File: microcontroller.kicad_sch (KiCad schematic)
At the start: 34 parts, among them U1 STM32H745XIH6

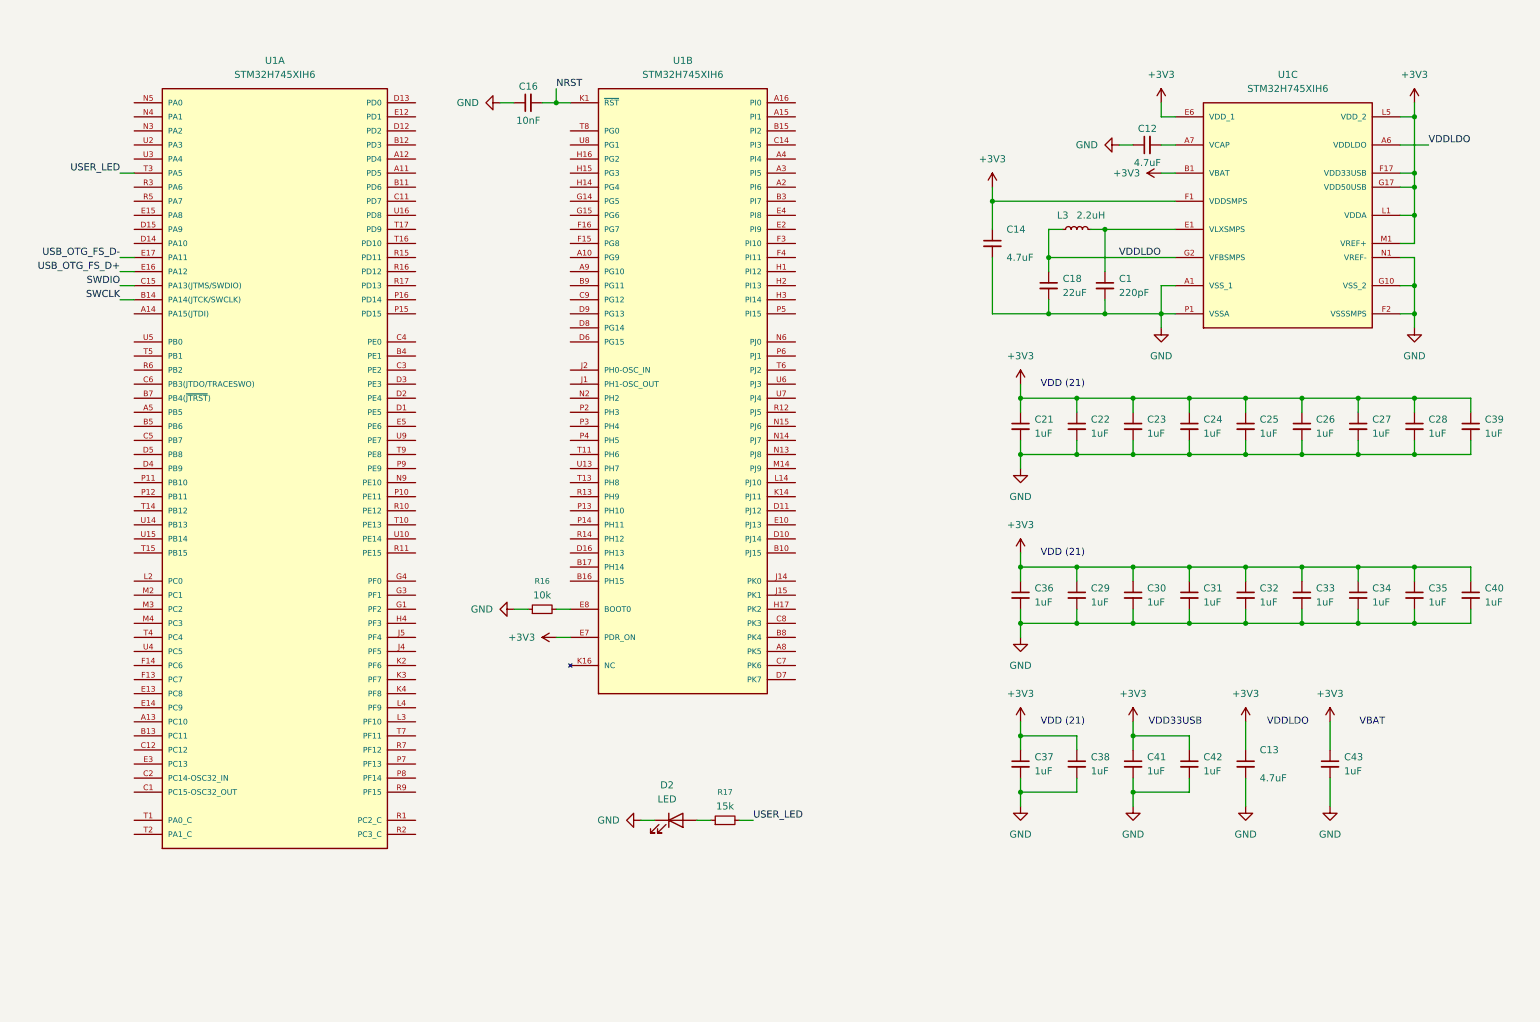
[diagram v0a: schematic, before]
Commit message: add fmc pins, stomp uart, fuel gauge i2c
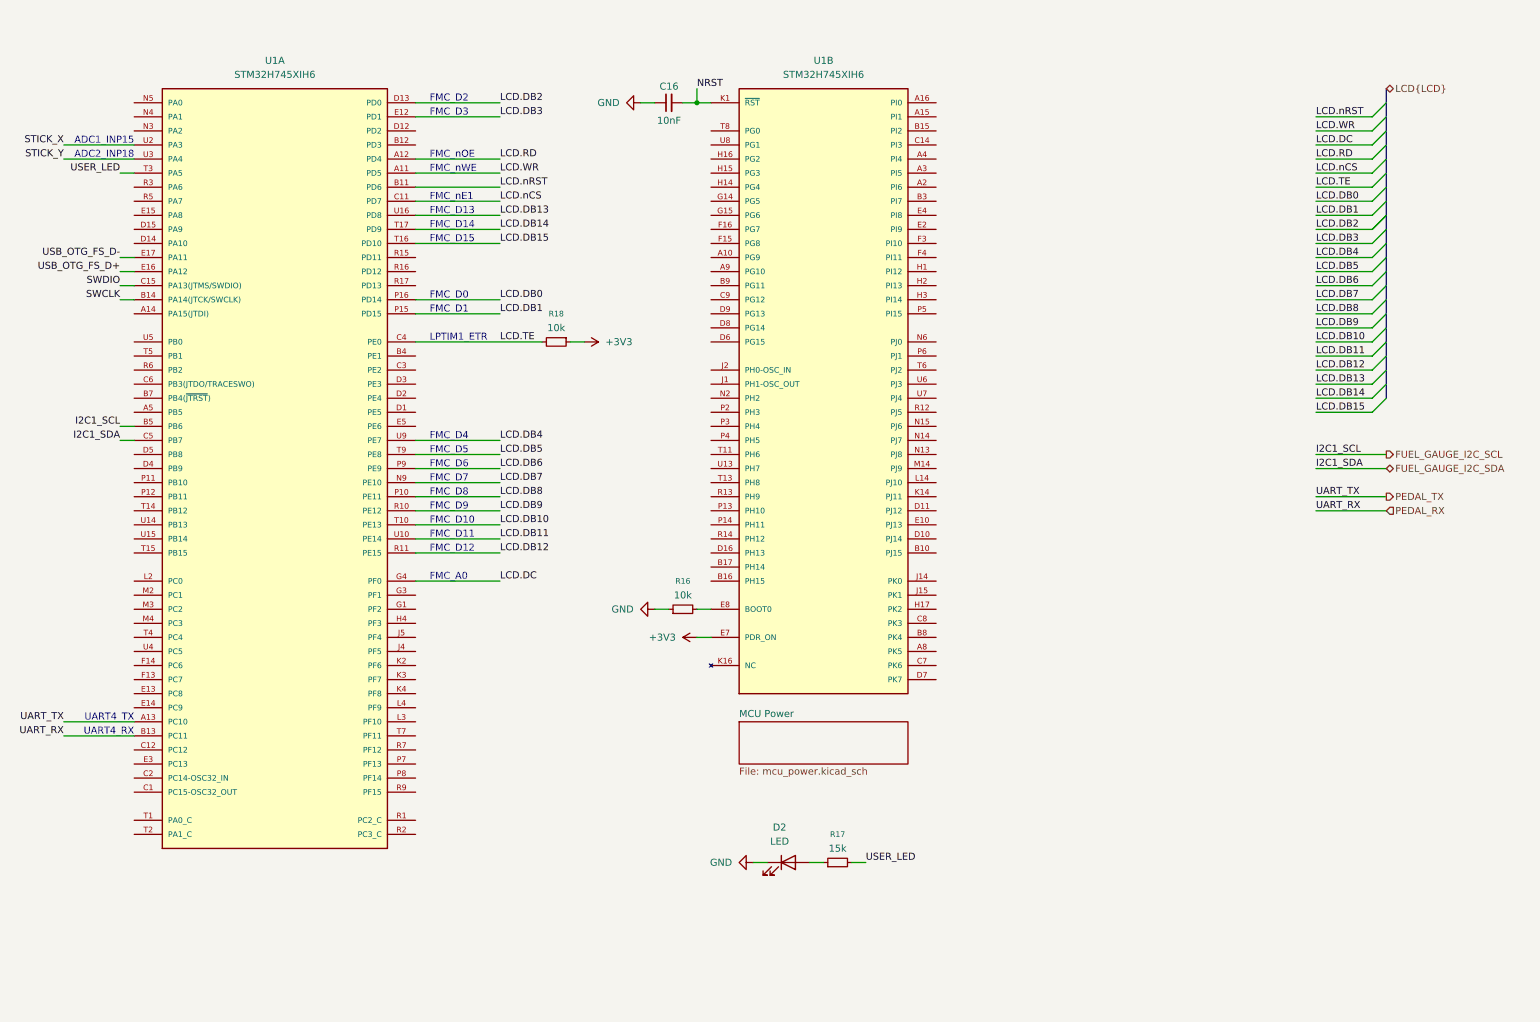
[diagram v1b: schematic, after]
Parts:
- removed C1: 220pF, Capacitor_SMD:C_0402_1005Metric, symbol Device:C_Small
- removed C12, C13, C14: 4.7uF, Capacitor_SMD:C_0402_1005Metric, symbol Device:C_Small
- removed C18: 22uF, Capacitor_SMD:C_0805_2012Metric, symbol Device:C_Small
- removed C21, C22, C23, C24, C25, C26, C27, C28, C29, C30, C31, C32, C33, C34, C35, C36, C37, C38, C39, C40, C41, C42, C43: 1uF, Capacitor_SMD:C_0402_1005Metric, symbol Device:C_Small
- removed L3: 2.2uH, Inductor_SMD:L_0805_2012Metric, symbol Device:L_Small
- removed unit 3 of U1
- added R18: 10k, Resistor_SMD:R_0402_1005Metric, symbol Device:R_Small
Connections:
- net +3V3: now also R18.1
- net LCD.WR: now reaches U1.A11 (PD5)
- net LCD.RD: now reaches U1.A12 (PD4)
- net PEDAL_TX: now reaches U1.A13 (PC10)
- net LCD.nRST: now reaches U1.B11 (PD6)
- net PEDAL_RX: now reaches U1.B13 (PC11)
- net FUEL_GAUGE_I2C_SCL: now reaches U1.B5 (PB6)
- net LCD.nCS: now reaches U1.C11 (PD7)
- net LCD.TE: now reaches U1.C4 (PE0)
- net LCD.TE: now also R18.2
- net FUEL_GAUGE_I2C_SDA: now reaches U1.C5 (PB7)
- net LCD.DB2: now reaches U1.D13 (PD0)
- net LCD.DB3: now reaches U1.E12 (PD1)
- net LCD.DC: now reaches U1.G4 (PF0)
- net LCD.DB7: now reaches U1.N9 (PE10)
- net LCD.DB8: now reaches U1.P10 (PE11)
- net LCD.DB1: now reaches U1.P15 (PD15)
- net LCD.DB0: now reaches U1.P16 (PD14)
- net LCD.DB6: now reaches U1.P9 (PE9)
- net LCD.DB9: now reaches U1.R10 (PE12)
- net LCD.DB12: now reaches U1.R11 (PE15)
- net LCD.DB10: now reaches U1.T10 (PE13)
- net LCD.DB15: now reaches U1.T16 (PD10)
- net LCD.DB14: now reaches U1.T17 (PD9)
- net LCD.DB5: now reaches U1.T9 (PE8)
- net LCD.DB11: now reaches U1.U10 (PE14)
- net LCD.DB13: now reaches U1.U16 (PD8)
- net STICK_X: now reaches U1.U2 (PA3)
- net STICK_Y: now reaches U1.U3 (PA4)
- net LCD.DB4: now reaches U1.U9 (PE7)
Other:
- added sheet MCU Power (mcu_power.kicad_sch)
- note added: "ADC1_INP15"
- note added: "ADC2_INP18"
- note added: "FMC_A0"
- note added: "FMC_D0"
- note added: "FMC_D1"
- note added: "FMC_D10"
- note added: "FMC_D11"
- note added: "FMC_D12"
- note added: "FMC_D13"
- note added: "FMC_D14"
- note added: "FMC_D15"
- note added: "FMC_D2"
- note added: "FMC_D3"
- note added: "FMC_D4"
- note added: "FMC_D5"
- note added: "FMC_D6"
- note added: "FMC_D7"
- note added: "FMC_D8"
- note added: "FMC_D9"
- note added: "FMC_nE1"
- note added: "FMC_nOE"
- note added: "FMC_nWE"
- note added: "LPTIM1_ETR"
- note added: "UART4_RX"
- note added: "UART4_TX"
- note removed: "VBAT"
- note removed: "VDD (21)"
- note removed: "VDD33USB"
- note removed: "VDDLDO"
- moved on the sheet: C16, D2, R16, R17, U1B

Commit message: update ioc
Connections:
- net USB_OTG_FS_D+ renamed USB_D+
- net USB_OTG_FS_D- renamed USB_D-

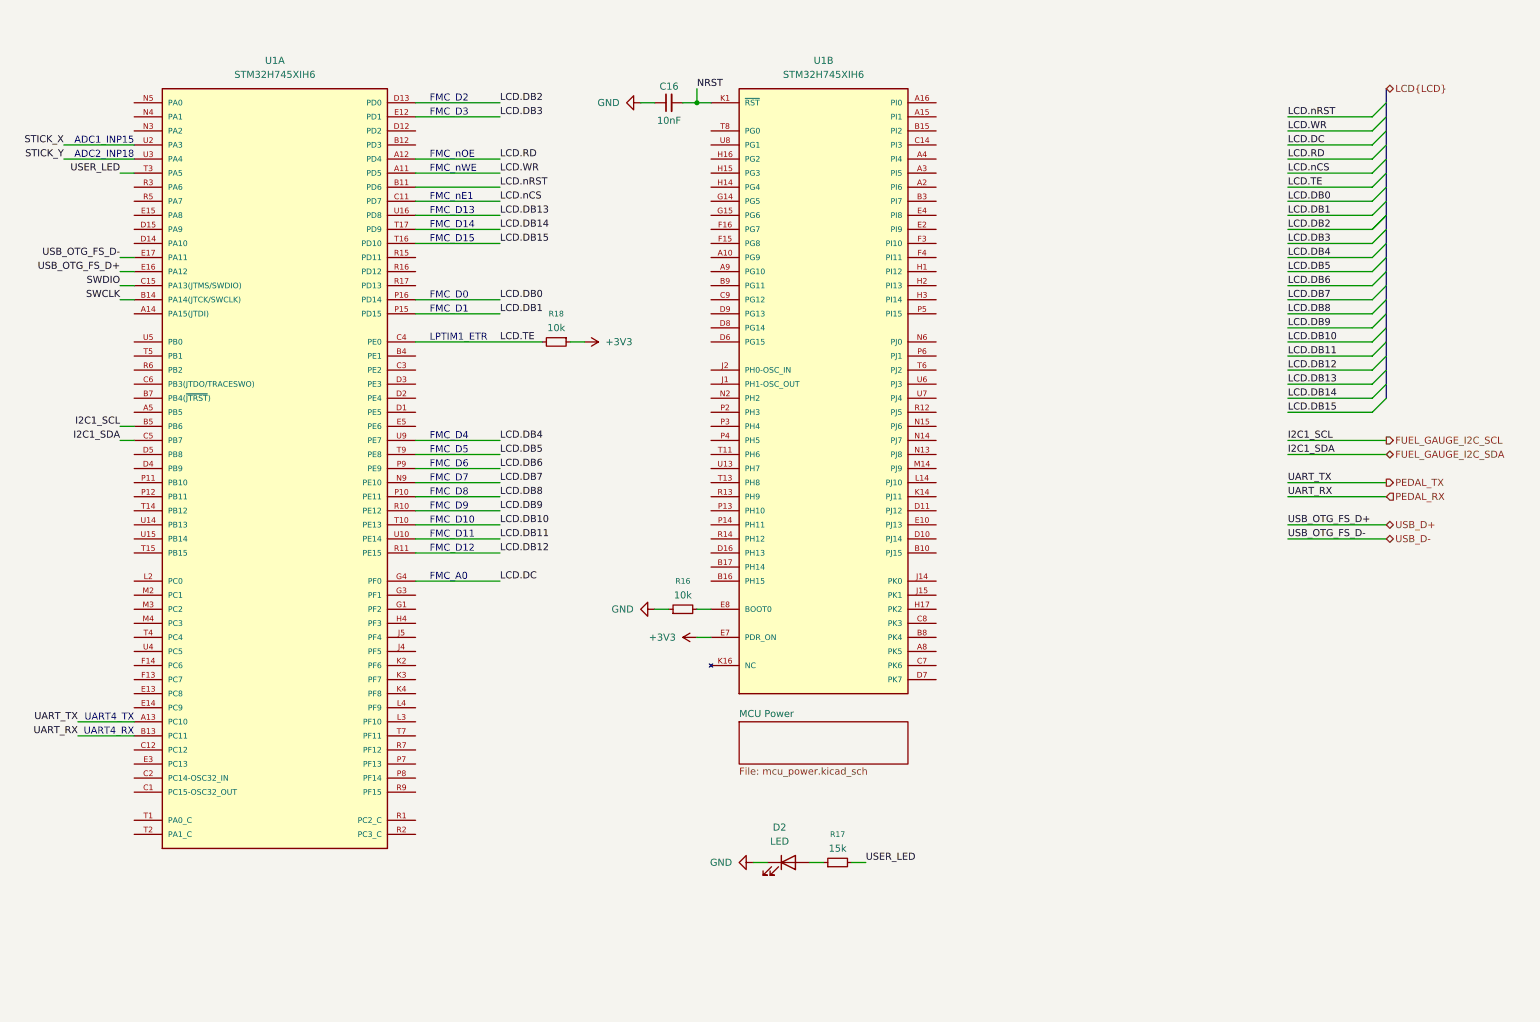
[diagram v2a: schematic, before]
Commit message: add a bunch of peripherals
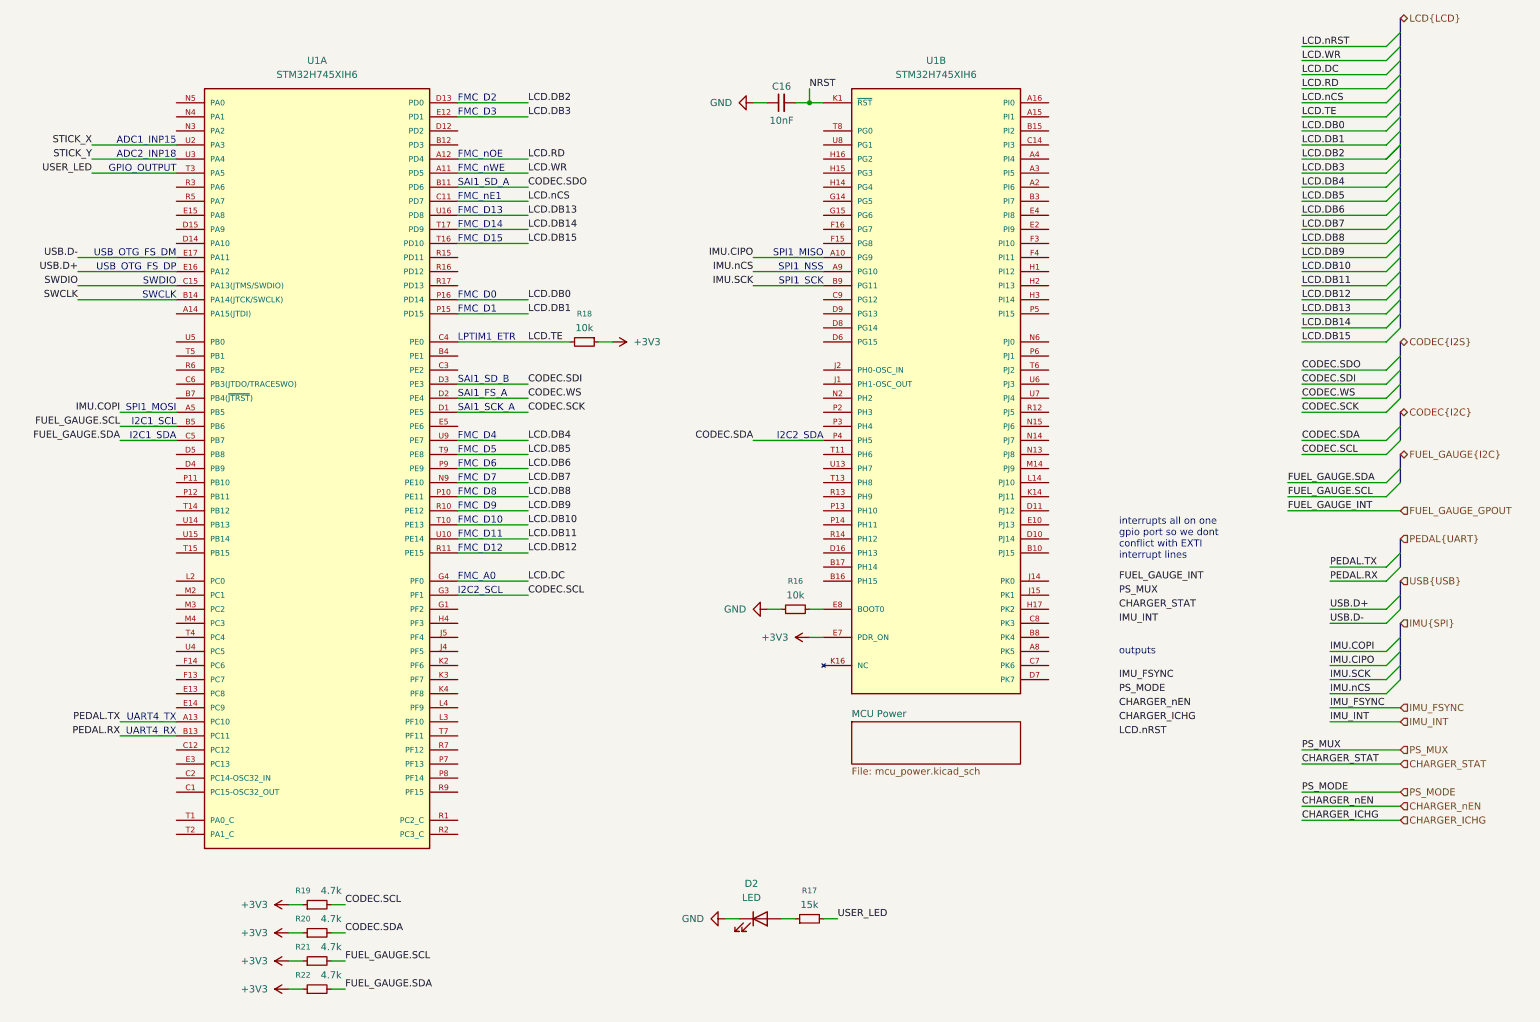
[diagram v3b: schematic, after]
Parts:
- added R19, R20, R21, R22: 4.7k, Resistor_SMD:R_0402_1005Metric, symbol Device:R_Small
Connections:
- net +3V3: now also R19.1, R20.1, R21.1, R22.1
- net LCD.nRST: no longer U1.B11 (PD6)
- net IMU.COPI: now reaches U1.A5 (PB5)
- net CODEC.SCK: now reaches U1.D1 (PE5)
- net CODEC.WS: now reaches U1.D2 (PE4)
- net CODEC.SDI: now reaches U1.D3 (PE3)
- net CODEC.SCL: now reaches U1.G3 (PF1)
- net CODEC.SCL: now also R19.2
- net IMU.CIPO: now reaches U1.A10 (PG9)
- net IMU.nCS: now reaches U1.A9 (PG10)
- net IMU.SCK: now reaches U1.B9 (PG11)
- net CODEC.SDA: now reaches U1.P4 (PH5)
- net CODEC.SDA: now also R20.2
- net FUEL_GAUGE_I2C_SCL renamed FUEL_GAUGE.SCL
- net FUEL_GAUGE.SCL: now also R21.2
- net FUEL_GAUGE_I2C_SDA renamed FUEL_GAUGE.SDA
- net FUEL_GAUGE.SDA: now also R22.2
- net PEDAL_RX renamed PEDAL.RX
- net PEDAL_TX renamed PEDAL.TX
- net USB_D+ renamed USB.D+
- net USB_D- renamed USB.D-
- new net CODEC.SDO: U1.B11 (PD6)
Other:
- note added: "GPIO_OUTPUT"
- note added: "I2C1_SCL"
- note added: "I2C1_SDA"
- note added: "I2C2_SCL"
- note added: "I2C2_SDA"
- note added: "SAI1_FS_A"
- note added: "SAI1_SCK_A"
- note added: "SAI1_SD_A"
- note added: "SAI1_SD_B"
- note added: "SPI1_MISO"
- note added: "SPI1_MOSI"
- note added: "SPI1_NSS"
- note added: "SPI1_SCK"
- note added: "SWCLK"
- note added: "SWDIO"
- note added: "USB_OTG_FS_DM"
- note added: "USB_OTG_FS_DP"
- note added: "interrupts all on one gpio port so we dont conflict with EXTI interrupt lines"
- note added: "outputs"
- moved on the sheet: C16, D2, R16, R17, R18, U1A, U1B

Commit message: add all external signals
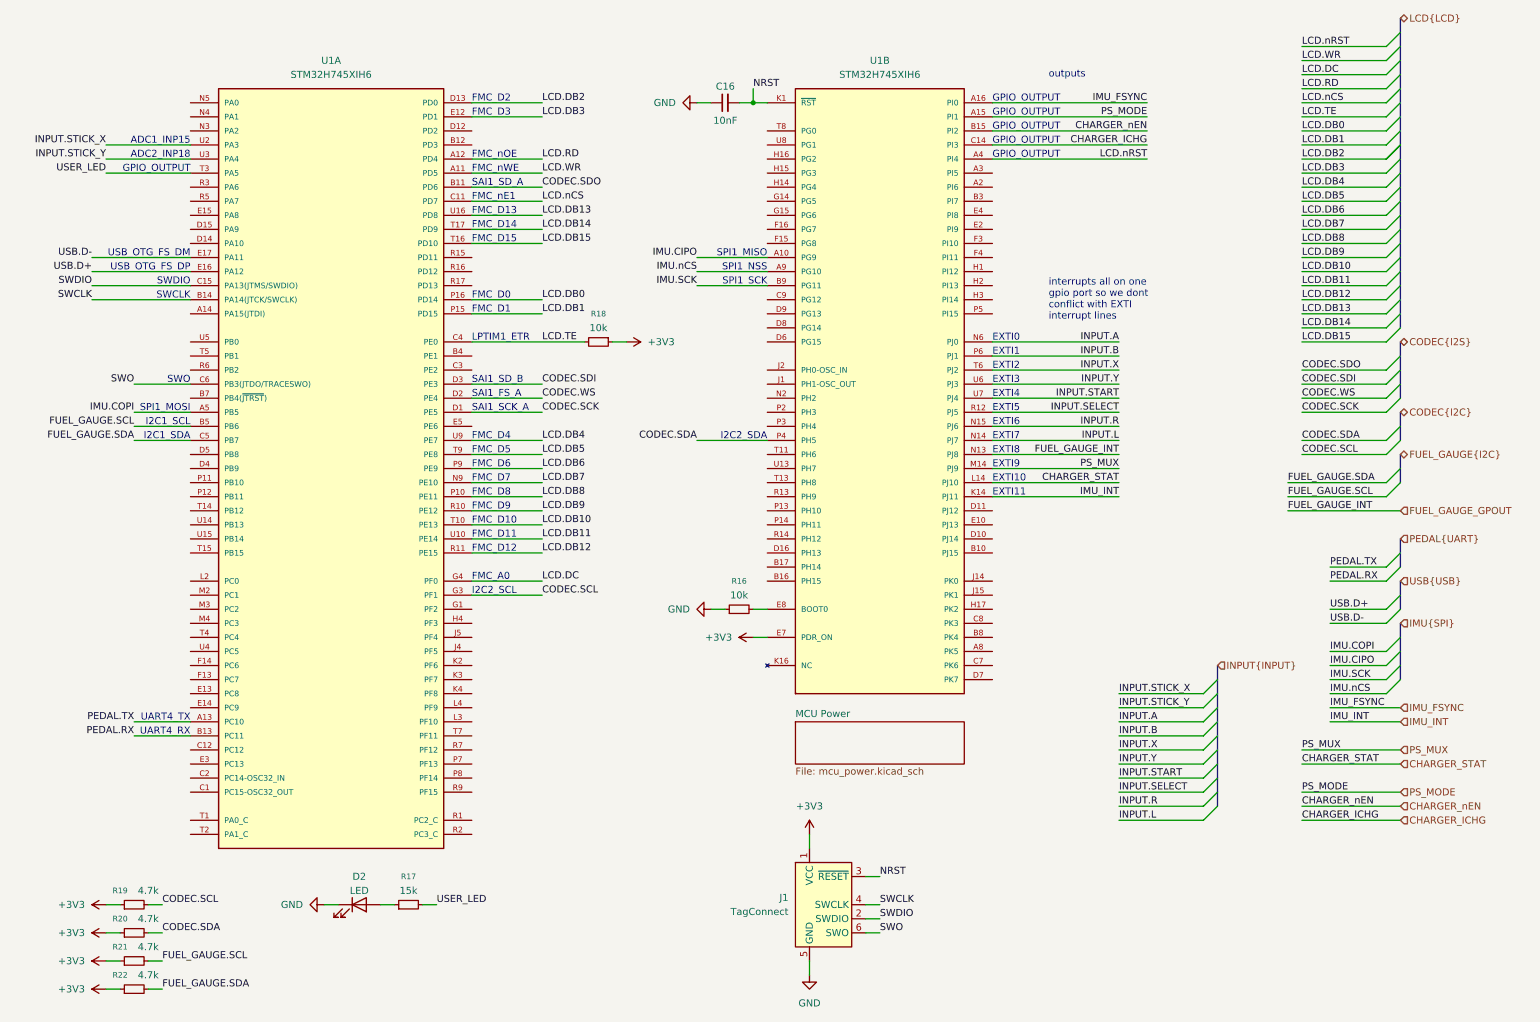
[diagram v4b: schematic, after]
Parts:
- added J1: TagConnect, Connector:Tag-Connect_TC2030-IDC-NL_2x03_P1.27mm_Vertical, symbol Connector:Conn_ARM_SWD_TagConnect_TC2030-NL
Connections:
- net +3V3: now also J1.1 (VCC)
- net CHARGER_ICHG: now also U1.C14 (PI3)
- net CHARGER_STAT: now also U1.L14 (PJ10)
- net CHARGER_nEN: now also U1.B15 (PI2)
- net FUEL_GAUGE_GPOUT: now also U1.N13 (PJ8)
- net GND: now also J1.5 (GND)
- net IMU_FSYNC: now also U1.A16 (PI0)
- net IMU_INT: now also U1.K14 (PJ11)
- net LCD.nRST: now also U1.A4 (PI4)
- net NRST: now also J1.3 (~{RESET})
- net PS_MODE: now also U1.A15 (PI1)
- net PS_MUX: now also U1.M14 (PJ9)
- net SWCLK: now also J1.4 (SWCLK)
- net SWDIO: now also J1.2 (SWDIO)
- net SWO: now reaches U1.C6 (PB3(JTDO/TRACESWO))
- net SWO: now also J1.6 (SWO)
- net INPUT.L: now reaches U1.N14 (PJ7)
- net INPUT.R: now reaches U1.N15 (PJ6)
- net INPUT.A: now reaches U1.N6 (PJ0)
- net INPUT.B: now reaches U1.P6 (PJ1)
- net INPUT.SELECT: now reaches U1.R12 (PJ5)
- net INPUT.X: now reaches U1.T6 (PJ2)
- net INPUT.Y: now reaches U1.U6 (PJ3)
- net INPUT.START: now reaches U1.U7 (PJ4)
- net STICK_X renamed INPUT.STICK_X
- net STICK_Y renamed INPUT.STICK_Y
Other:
- note added: "EXTI0"
- note added: "EXTI1"
- note added: "EXTI10"
- note added: "EXTI11"
- note added: "EXTI2"
- note added: "EXTI3"
- note added: "EXTI4"
- note added: "EXTI5"
- note added: "EXTI6"
- note added: "EXTI7"
- note added: "EXTI8"
- note added: "EXTI9"
- note added: "SWO"
- moved on the sheet: C16, D2, R16, R17, R18, R19, R20, R21, R22, U1A, U1B
